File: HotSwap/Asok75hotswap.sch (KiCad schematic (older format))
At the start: 259 parts, among them J1 AVR-ISP-6, SW1 SW_Push, U1 ATmega32U4-MU, U2 PRTR5V0U2X, Y1 16MHz

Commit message: Removed extra symbols in schematic in hotswap variant
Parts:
- removed D12, D30, D52, D77: SOD-123, random-keyboard-parts:D_SOD-123-Pretty, symbol Device:D_Small
- removed MX_BCKSP2, MX_BCKSP3, MX_LSHIFT3, MX_LWIN2, MX_\2: MX-LED, MX_Only:MXOnly-1U-Hotswap, symbol MX_Alps_Hybrid:MX-LED
- removed MX_CAPS2, MX_LSHIFT2, MX_SPACE4: MX-LED, MX_Only:MXOnly-1.25U-Hotswap, symbol MX_Alps_Hybrid:MX-LED
- removed MX_ENTER2: MX-LED, MX_Only:MXOnly-ISO-ROTATED-ReversedStabilizers-NoLED, symbol MX_Alps_Hybrid:MX-LED
- removed MX_LALT2, MX_LALT3, MX_LCTRL2, MX_RALT2, MX_RCTRL2: MX-LED, MX_Only:MXOnly-1.5U-Hotswap, symbol MX_Alps_Hybrid:MX-LED
- removed MX_SPACE2, MX_SPACE3: MX-LED, MX_Only:MXOnly-7U-Hotswap-ReversedStabilizers, symbol MX_Alps_Hybrid:MX-LED
- removed MX_SPACE5: MX-LED, MX_Only:MXOnly-2.75U-Hotswap-ReversedStabilizers, symbol MX_Alps_Hybrid:MX-LED
- removed MX_SPACE6: MX-LED, MX_Only:MXOnly-2.25U-Hotswap-ReversedStabilizers, symbol MX_Alps_Hybrid:MX-LED
- C1: renamed from C21; footprint Capacitor_SMD:C_0805_2012Metric -> Capacitor_SMD:C_0603_1608Metric
- C10: renamed from C12; footprint Capacitor_SMD:C_0805_2012Metric -> Capacitor_SMD:C_0603_1608Metric
- C11: footprint Capacitor_SMD:C_0805_2012Metric -> Capacitor_SMD:C_0603_1608Metric
- C12: renamed from C10; footprint Capacitor_SMD:C_0805_2012Metric -> Capacitor_SMD:C_0603_1608Metric
- C13: renamed from C9; footprint Capacitor_SMD:C_0805_2012Metric -> Capacitor_SMD:C_0603_1608Metric
- C14: renamed from C8; footprint Capacitor_SMD:C_0805_2012Metric -> Capacitor_SMD:C_0603_1608Metric
- C15: renamed from C1; footprint Capacitor_SMD:C_0805_2012Metric -> Capacitor_SMD:C_0603_1608Metric
- C16: renamed from C2; footprint Capacitor_SMD:C_0805_2012Metric -> Capacitor_SMD:C_0603_1608Metric
- C17: renamed from C3; footprint Capacitor_SMD:C_0805_2012Metric -> Capacitor_SMD:C_0603_1608Metric
- C18: renamed from C4; footprint Capacitor_SMD:C_0805_2012Metric -> Capacitor_SMD:C_0603_1608Metric
- C19: renamed from C5; footprint Capacitor_SMD:C_0805_2012Metric -> Capacitor_SMD:C_0603_1608Metric
- C2: renamed from C20; footprint Capacitor_SMD:C_0805_2012Metric -> Capacitor_SMD:C_0603_1608Metric
- C20: renamed from C6; footprint Capacitor_SMD:C_0805_2012Metric -> Capacitor_SMD:C_0603_1608Metric
- C21: renamed from C7; footprint Capacitor_SMD:C_0805_2012Metric -> Capacitor_SMD:C_0603_1608Metric
- C3: renamed from C19; footprint Capacitor_SMD:C_0805_2012Metric -> Capacitor_SMD:C_0603_1608Metric
- C4: renamed from C18; footprint Capacitor_SMD:C_0805_2012Metric -> Capacitor_SMD:C_0603_1608Metric
- C5: renamed from C17; footprint Capacitor_SMD:C_0805_2012Metric -> Capacitor_SMD:C_0603_1608Metric
- C6: renamed from C16; footprint Capacitor_SMD:C_0805_2012Metric -> Capacitor_SMD:C_0603_1608Metric
- C7: renamed from C15; footprint Capacitor_SMD:C_0805_2012Metric -> Capacitor_SMD:C_0603_1608Metric
- C8: renamed from C14; footprint Capacitor_SMD:C_0805_2012Metric -> Capacitor_SMD:C_0603_1608Metric
- C9: renamed from C13; footprint Capacitor_SMD:C_0805_2012Metric -> Capacitor_SMD:C_0603_1608Metric
- R1, R2, R3: footprint Resistor_SMD:R_0805_2012Metric -> Resistor_SMD:R_0603_1608Metric
- R4: renamed from R7; footprint Resistor_SMD:R_0805_2012Metric -> Resistor_SMD:R_0603_1608Metric
- R5: renamed from R6; footprint Resistor_SMD:R_0805_2012Metric -> Resistor_SMD:R_0603_1608Metric
- R6: renamed from R5; footprint Resistor_SMD:R_0805_2012Metric -> Resistor_SMD:R_0603_1608Metric
- R7: renamed from R8; footprint Resistor_SMD:R_0805_2012Metric -> Resistor_SMD:R_0603_1608Metric
- R8: renamed from R9; footprint Resistor_SMD:R_0805_2012Metric -> Resistor_SMD:R_0603_1608Metric
- R9: renamed from R4; footprint Resistor_SMD:R_0805_2012Metric -> Resistor_SMD:R_0603_1608Metric
- renumbered D2 to D1, D11 to D10, D18 to D11, D13 to D12, D14 to D13, D15 to D14, D16 to D15, D17 to D16, D24 to D17, D19 to D18, D20 to D19, D3 to D2, D21 to D20, D22 to D21, D23 to D22, D29 to D23, D25 to D24, D26 to D25, D27 to D26, D28 to D27, D35 to D28, D31 to D29, D4 to D3, D32 to D30, D33 to D31, D34 to D32, D40 to D33, D36 to D34, D37 to D35, D38 to D36, D39 to D37, D46 to D38, D41 to D39, D5 to D4, D42 to D40, D43 to D41, D44 to D42, D45 to D43, D51 to D44, D47 to D45, D48 to D46, D49 to D47, D50 to D48, D57 to D49, D6 to D5, D53 to D50, D54 to D51, D55 to D52, D56 to D53, D63 to D54, D58 to D55, D59 to D56, D60 to D57, D61 to D58, D62 to D59, D7 to D6, D69 to D60, D64 to D61, D65 to D62, D66 to D63, D67 to D64, D68 to D65, D74 to D66, D70 to D67, D71 to D68, D72 to D69, D8 to D7, D73 to D70, D80 to D71, D81 to D72, D75 to D73, D76 to D74, D79 to D75, D78 to D76, D82 to D77, D83 to D78, D84 to D79, D9 to D8, D85 to D80, D89 to D81, D90 to D82, D91 to D83, D86 to D84, D87 to D85, D88 to D86, D1 to D87, D10 to D9, LED12 to LED10, LED6 to LED11, LED13 to LED12, LED7 to LED13, LED8 to LED2, LED2 to LED3, LED9 to LED4, LED3 to LED5, LED10 to LED6, LED4 to LED7, LED11 to LED8, LED5 to LED9, MX_#0 to MX_#10, U2 to U1, U1 to U2
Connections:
- net COL0: now also MX_Z1.1 (COL)
- net COL1: now also MX_C1.1 (COL); no longer MX_Z1.1 (COL)
- net COL2: now also MX_B1.1 (COL); no longer MX_C1.1 (COL)
- net COL3: now also MX_M1.1 (COL); no longer MX_B1.1 (COL)
- net COL4: now also MX_.1.1 (COL); no longer MX_M1.1 (COL)
- net COL5: now also MX_RSHIFT1.1 (COL); no longer MX_.1.1 (COL)
- net COL6: now also MX_BCKSP1.1 (COL), MX_DOWN1.1 (COL), MX_UP1.1 (COL); no longer MX_RSHIFT1.1 (COL)
- net COL7: no longer MX_BCKSP1.1 (COL), MX_DOWN1.1 (COL), MX_UP1.1 (COL)
- net ROW0: now also D78.1 (K)
- net ROW1: no longer D78.1 (K)
- net ROW10: now also D83.1 (K); no longer D77.1 (K)
- net ROW11: now also D77.1 (K); no longer D83.1 (K)
- net ROW2: now also D79.1 (K); no longer D75.1 (K)
- net ROW3: now also D75.1 (K); no longer D79.1 (K)
- net ROW4: now also D80.1 (K)
- net ROW5: no longer D80.1 (K)
- net ROW6: now also D81.1 (K)
- net ROW7: no longer D81.1 (K)
- net ROW8: now also D17.1 (K), D28.1 (K), D38.1 (K), D49.1 (K), D60.1 (K), D82.1 (K); no longer D11.1 (K), D23.1 (K), D33.1 (K), D44.1 (K), D54.1 (K), D66.1 (K)
- net ROW9: now also D11.1 (K), D23.1 (K), D33.1 (K), D44.1 (K), D54.1 (K), D66.1 (K); no longer D17.1 (K), D28.1 (K), D38.1 (K), D49.1 (K), D60.1 (K), D82.1 (K)
- net LEDMOS: now reaches U2.12 (PB7)
- net at MX_A1.3 (LED): now also MX_Z1.3 (LED)
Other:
- note added: "LED MOSFET\n"
- moved on the sheet: D11, D17, D23, D28, D33, D38, D44, D49, D54, D60, D66, D72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

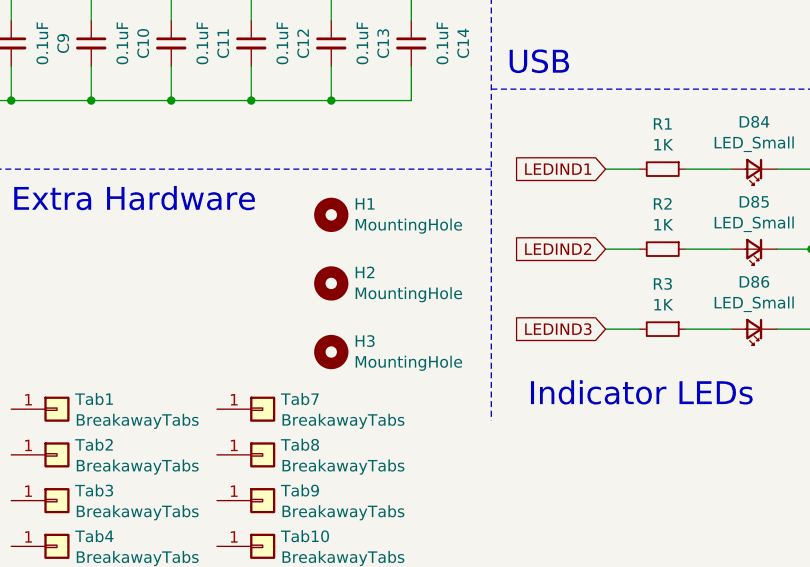
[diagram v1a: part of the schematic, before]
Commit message: Updated underglow LED footprint
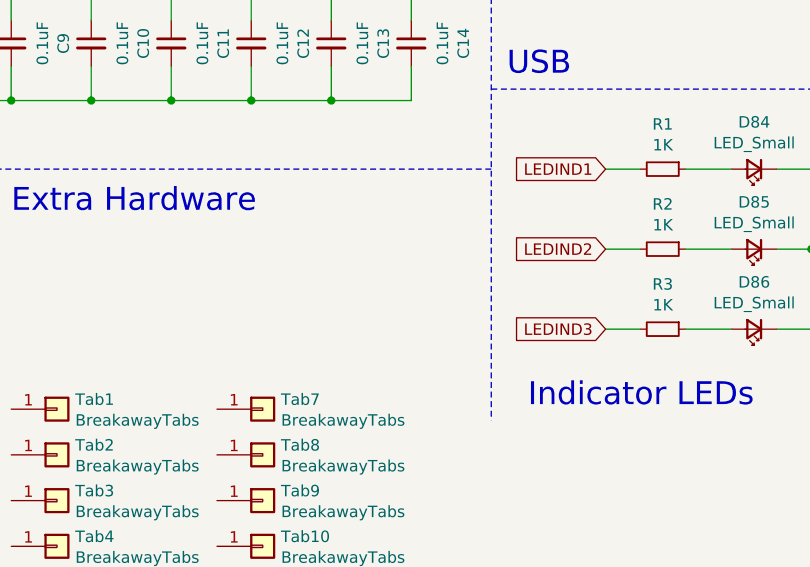
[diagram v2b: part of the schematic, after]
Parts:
- removed H1, H2, H3: MountingHole, mounting_hole:mounting, symbol Mechanical:MountingHole
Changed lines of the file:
@@
-	1    0    0    -1
-$EndComp
-$Comp
-L Mechanical:MountingHole H3
-U 1 1 5EBE734B
-P 11450 9650
-F 0 "H3" H 11550 9696 50  0000 L CNN
-F 1 "MountingHole" H 11550 9605 50  0000 L CNN
-F 2 "mounting_hole:mounting" H 11450 9650 50  0001 C CNN
-F 3 "~" H 11450 9650 50  0001 C CNN
-	1    11450 9650
-	1    0    0    -1
-$EndComp
-$Comp
-L Mechanical:MountingHole H2
-U 1 1 5EAF9D7C
-P 11450 9350
-F 0 "H2" H 11550 9396 50  0000 L CNN
-F 1 "MountingHole" H 11550 9305 50  0000 L CNN
-F 2 "mounting_hole:mounting" H 11450 9350 50  0001 C CNN
-F 3 "~" H 11450 9350 50  0001 C CNN
-	1    11450 9350
-	1    0    0    -1
-$EndComp
-$Comp
-L Mechanical:MountingHole H1
-U 1 1 5EAF6EE2
-P 11450 9050
-F 0 "H1" H 11550 9096 50  0000 L CNN
-F 1 "MountingHole" H 11550 9005 50  0000 L CNN
-F 2 "mounting_hole:mounting" H 11450 9050 50  0001 C CNN
-F 3 "~" H 11450 9050 50  0001 C CNN
-	1    11450 9050
 	1    0    0    -1
 $EndComp

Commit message: Routed USB and MCU area for hotswap version
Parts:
- removed D87: Schottky, random-keyboard-parts:D_SOD-123-Pretty, symbol Device:D_Schottky_Small
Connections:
- net +5V: now also F1.1
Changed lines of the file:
@@
 	1    0    0    -1
 $EndComp
-$Comp
-L Device:D_Schottky_Small D87
-U 1 1 617B5949
-P 14050 5800
-F 0 "D87" H 14050 5595 50  0000 C CNN
-F 1 "Schottky" H 14050 5686 50  0000 C CNN
-F 2 "random-keyboard-parts:D_SOD-123-Pretty" V 14050 5800 50  0001 C CNN
-F 3 "~" V 14050 5800 50  0001 C CNN
-	1    14050 5800
-	-1   0    0    1
-$EndComp
-Wire Wire Line
-	13800 5800 13950 5800
-Wire Wire Line
-	14150 5800 14250 5800
 Wire Wire Line
 	14250 5800 14250 5700
@@
 Wire Wire Line
 	8900 2700 10200 2700
+Wire Wire Line
+	13800 5800 14250 5800
 $EndSCHEMATC

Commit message: Routed underglow LEDs
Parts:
- renumbered LED6 to LED10, LED8 to LED11, LED10 to LED12, LED12 to LED13, LED3 to LED2, LED5 to LED3, LED7 to LED4, LED9 to LED5, LED11 to LED6, LED13 to LED7, LED2 to LED8, LED4 to LED9
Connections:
- net COL0: no longer U2.32 (PC7)
- net COL1: no longer U2.31 (PC6)
- net COL2: no longer U2.30 (PB6)
- net COL3: no longer U2.29 (PB5)
- net COL4: no longer U2.28 (PB4)
- net COL5: no longer U2.27 (PD7)
- net COL6: no longer U2.26 (PD6)
- net COL7: no longer U2.25 (PD4)
- net LEDIND1: no longer U2.10 (PB2)
- net LEDIND2: no longer U2.9 (PB1)
- net LEDIND3: no longer U2.8 (PB0)
- net RGBLED: no longer U2.18 (PD0)
- net ROW0: no longer U2.1 (PE6)
- net ROW1: no longer U2.11 (PB3)
- net ROW10: no longer U2.20 (PD2)
- net ROW11: no longer U2.19 (PD1)
- net ROW2: no longer U2.41 (PF0)
- net ROW3: no longer U2.40 (PF1)
- net ROW4: no longer U2.39 (PF4)
- net ROW5: no longer U2.38 (PF5)
- net ROW6: no longer U2.37 (PF6)
- net ROW7: no longer U2.36 (PF7)
- net ROW8: no longer U2.21 (PD3)
- net ROW9: no longer U2.22 (PD5)
- net LEDMOS: no longer names the net of U2.12 (PB7)
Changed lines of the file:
@@
 Text Notes 8050 7700 0    100  ~ 0
 Underglow LEDs
-Text GLabel 15450 1900 2    50   Input ~ 0
-LEDMOS
 $Comp
 L power:GND #PWR017
@@
 Connection ~ 8650 8550
 Connection ~ 9000 8050
-Text GLabel 15450 2200 2    50   Input ~ 0
-COL0
-Text GLabel 15450 2100 2    50   Input ~ 0
-COL1
-Text GLabel 15450 1800 2    50   Input ~ 0
-COL2
-Text GLabel 15450 1700 2    50   Input ~ 0
-COL3
-Text GLabel 15450 1600 2    50   Input ~ 0
-COL4
-Text GLabel 15450 3100 2    50   Input ~ 0
-COL5
-Text GLabel 15450 3000 2    50   Input ~ 0
-COL6
-Text GLabel 15450 2800 2    50   Input ~ 0
-COL7
-Text GLabel 15450 2400 2    50   Input ~ 0
-RGBLED
-Text GLabel 15450 2600 2    50   Input ~ 0
-ROW10
-Text GLabel 15450 2500 2    50   Input ~ 0
-ROW11
-Text GLabel 15450 2900 2    50   Input ~ 0
-ROW9
-Text GLabel 15450 2700 2    50   Input ~ 0
-ROW8
-Text GLabel 15450 4100 2    50   Input ~ 0
-ROW7
-Text GLabel 15450 4000 2    50   Input ~ 0
-ROW6
-Text GLabel 15450 3900 2    50   Input ~ 0
-ROW5
-Text GLabel 15450 3800 2    50   Input ~ 0
-ROW4
-Text GLabel 15450 3600 2    50   Input ~ 0
-ROW2
-Text GLabel 15450 3700 2    50   Input ~ 0
-ROW3
-Text GLabel 15450 1500 2    50   Input ~ 0
-ROW1
-Text GLabel 15450 3400 2    50   Input ~ 0
-ROW0
-Text GLabel 15450 1400 2    50   Input ~ 0
-LEDIND1
-Text GLabel 15450 1300 2    50   Input ~ 0
-LEDIND2
-Text GLabel 15450 1200 2    50   Input ~ 0
-LEDIND3
 Text Notes 15850 1350 0    50   ~ 0
 SCK\n
@@
 $EndComp
 $Comp
-L asok75:SK6812-SIDEA-4020 LED3
+L asok75:SK6812-SIDEA-4020 LED2
 U 1 1 5F5065E5
 P 2650 9450
-F 0 "LED3" H 2650 9937 60  0000 C CNN
+F 0 "LED2" H 2650 9937 60  0000 C CNN
 F 1 "SK6812-SIDEA-4020" H 2650 9831 60  0000 C CNN
 F 2 "asok75:SK6812-SIDEA-4020" V 2600 9450 60  0001 C CNN
@@
 $EndComp
 $Comp
-L asok75:SK6812-SIDEA-4020 LED5
+L asok75:SK6812-SIDEA-4020 LED3
 U 1 1 5F50BC5A
 P 3950 9450
-F 0 "LED5" H 3950 9937 60  0000 C CNN
+F 0 "LED3" H 3950 9937 60  0000 C CNN
 F 1 "SK6812-SIDEA-4020" H 3950 9831 60  0000 C CNN
 F 2 "asok75:SK6812-SIDEA-4020" V 3900 9450 60  0001 C CNN
@@
 $EndComp
 $Comp
-L asok75:SK6812-SIDEA-4020 LED7
+L asok75:SK6812-SIDEA-4020 LED4
 U 1 1 5F5CE02B
 P 5250 9450
-F 0 "LED7" H 5250 9937 60  0000 C CNN
+F 0 "LED4" H 5250 9937 60  0000 C CNN
 F 1 "SK6812-SIDEA-4020" H 5250 9831 60  0000 C CNN
 F 2 "asok75:SK6812-SIDEA-4020" V 5200 9450 60  0001 C CNN
@@
 $EndComp
 $Comp
-L asok75:SK6812-SIDEA-4020 LED9
+L asok75:SK6812-SIDEA-4020 LED5
 U 1 1 5F68F568
 P 6550 9450
-F 0 "LED9" H 6550 9937 60  0000 C CNN
+F 0 "LED5" H 6550 9937 60  0000 C CNN
 F 1 "SK6812-SIDEA-4020" H 6550 9831 60  0000 C CNN
 F 2 "asok75:SK6812-SIDEA-4020" V 6500 9450 60  0001 C CNN
@@
 $EndComp
 $Comp
-L asok75:SK6812-SIDEA-4020 LED11
+L asok75:SK6812-SIDEA-4020 LED6
 U 1 1 5F750D68
 P 7850 9450
-F 0 "LED11" H 7850 9937 60  0000 C CNN
+F 0 "LED6" H 7850 9937 60  0000 C CNN
 F 1 "SK6812-SIDEA-4020" H 7850 9831 60  0000 C CNN
 F 2 "asok75:SK6812-SIDEA-4020" V 7800 9450 60  0001 C CNN
@@
 $EndComp
 $Comp
-L asok75:SK6812-SIDEA-4020 LED13
+L asok75:SK6812-SIDEA-4020 LED7
 U 1 1 5F811FD6
 P 9150 9450
-F 0 "LED13" H 9150 9937 60  0000 C CNN
+F 0 "LED7" H 9150 9937 60  0000 C CNN
 F 1 "SK6812-SIDEA-4020" H 9150 9831 60  0000 C CNN
 F 2 "asok75:SK6812-SIDEA-4020" V 9100 9450 60  0001 C CNN
@@
 $EndComp
 $Comp
-L asok75:SK6812-SIDEA-4020 LED4
+L asok75:SK6812-SIDEA-4020 LED9
 U 1 1 5FA6047D
 P 2650 10450
-F 0 "LED4" H 2650 10937 60  0000 C CNN
+F 0 "LED9" H 2650 10937 60  0000 C CNN
 F 1 "SK6812-SIDEA-4020" H 2650 10831 60  0000 C CNN
 F 2 "asok75:SK6812-SIDEA-4020" V 2600 10450 60  0001 C CNN
@@
 $EndComp
 $Comp
-L asok75:SK6812-SIDEA-4020 LED6
+L asok75:SK6812-SIDEA-4020 LED10
 U 1 1 5FA60483
 P 3950 10450
-F 0 "LED6" H 3950 10937 60  0000 C CNN
+F 0 "LED10" H 3950 10937 60  0000 C CNN
 F 1 "SK6812-SIDEA-4020" H 3950 10831 60  0000 C CNN
 F 2 "asok75:SK6812-SIDEA-4020" V 3900 10450 60  0001 C CNN
@@
 $EndComp
 $Comp
-L asok75:SK6812-SIDEA-4020 LED8
+L asok75:SK6812-SIDEA-4020 LED11
 U 1 1 5FA60489
 P 5250 10450
-F 0 "LED8" H 5250 10937 60  0000 C CNN
+F 0 "LED11" H 5250 10937 60  0000 C CNN
 F 1 "SK6812-SIDEA-4020" H 5250 10831 60  0000 C CNN
 F 2 "asok75:SK6812-SIDEA-4020" V 5200 10450 60  0001 C CNN
@@
 $EndComp
 $Comp
-L asok75:SK6812-SIDEA-4020 LED10
+L asok75:SK6812-SIDEA-4020 LED12
 U 1 1 5FA6048F
 P 6550 10450
-F 0 "LED10" H 6550 10937 60  0000 C CNN
+F 0 "LED12" H 6550 10937 60  0000 C CNN
 F 1 "SK6812-SIDEA-4020" H 6550 10831 60  0000 C CNN
 F 2 "asok75:SK6812-SIDEA-4020" V 6500 10450 60  0001 C CNN
@@
 $EndComp
 $Comp
-L asok75:SK6812-SIDEA-4020 LED12
+L asok75:SK6812-SIDEA-4020 LED13
 U 1 1 5FA60495
 P 7850 10450
-F 0 "LED12" H 7850 10937 60  0000 C CNN
+F 0 "LED13" H 7850 10937 60  0000 C CNN
 F 1 "SK6812-SIDEA-4020" H 7850 10831 60  0000 C CNN
 F 2 "asok75:SK6812-SIDEA-4020" V 7800 10450 60  0001 C CNN
@@
 $EndComp
 $Comp
-L asok75:SK6812-SIDEA-4020 LED2
+L asok75:SK6812-SIDEA-4020 LED8
 U 1 1 5FA604A1
 P 1350 10450
-F 0 "LED2" H 1350 10937 60  0000 C CNN
+F 0 "LED8" H 1350 10937 60  0000 C CNN
 F 1 "SK6812-SIDEA-4020" H 1350 10831 60  0000 C CNN
 F 2 "asok75:SK6812-SIDEA-4020" V 1300 10450 60  0001 C CNN

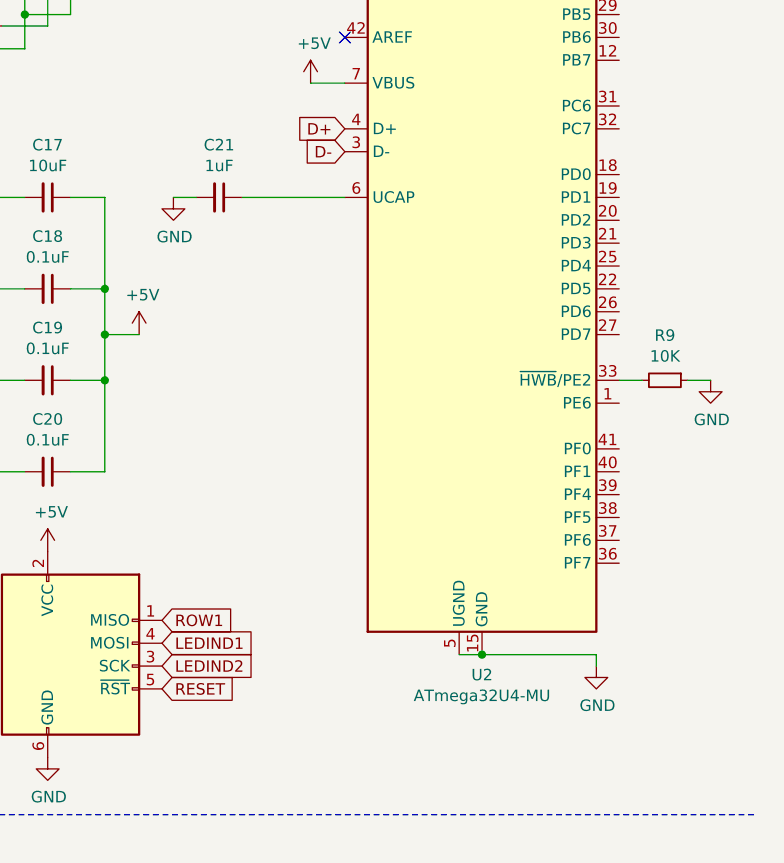
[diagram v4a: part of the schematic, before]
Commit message: Finished routing underglow LED power traces
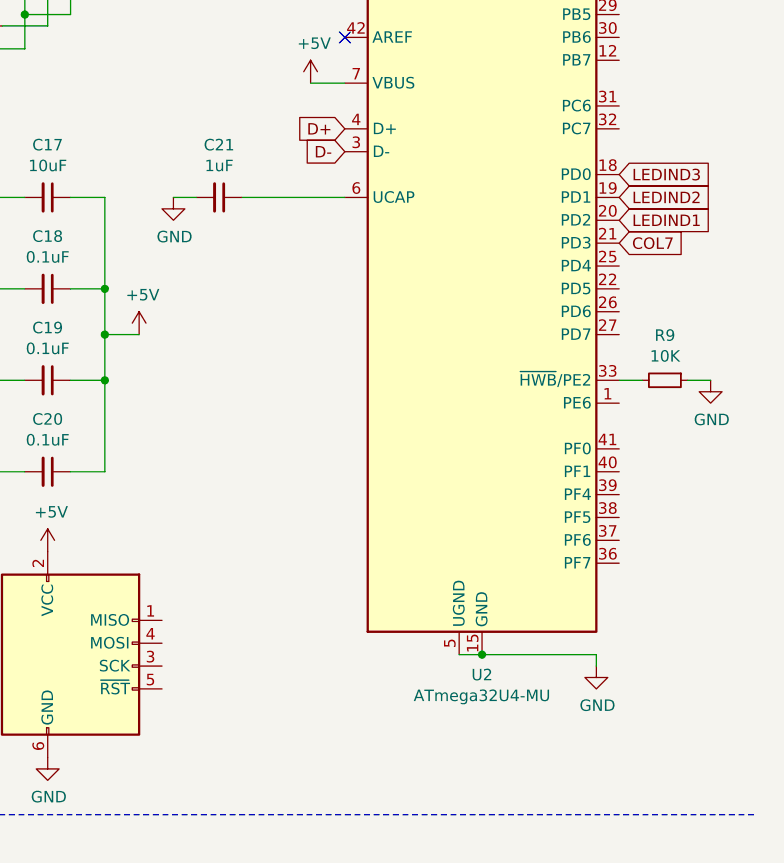
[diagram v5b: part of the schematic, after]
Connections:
- net COL7: now also U2.21 (PD3)
- net LEDIND1: now also U2.20 (PD2); no longer J1.4 (MOSI)
- net LEDIND2: now also U2.19 (PD1); no longer J1.3 (SCK)
- net LEDIND3: now also U2.18 (PD0)
- net RESET: no longer J1.5 (~RST)
- net ROW1: no longer J1.1 (MISO)
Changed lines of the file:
@@
 	1    0    0    -1
 $EndComp
-Text GLabel 13450 4650 2    50   Input ~ 0
-RESET
-Text GLabel 13450 4550 2    50   Input ~ 0
-LEDIND2
-Text GLabel 13450 4450 2    50   Input ~ 0
-LEDIND1
-Text GLabel 13450 4350 2    50   Input ~ 0
-ROW1
 $Comp
 L power:GND #PWR08
@@
 Wire Wire Line
 	13800 5800 14250 5800
+Text GLabel 15450 2600 2    50   Input ~ 0
+LEDIND1
+Text GLabel 15450 2700 2    50   Input ~ 0
+COL7
+Text GLabel 15450 2500 2    50   Input ~ 0
+LEDIND2
+Text GLabel 15450 2400 2    50   Input ~ 0
+LEDIND3
 $EndSCHEMATC

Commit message: Finished routing hotswap version
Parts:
- removed Tab10, Tab11, Tab12, Tab13, Tab5, Tab6, Tab7, Tab8, Tab9: BreakawayTabs, random-keyboard-parts:breakaway-mousebites, symbol Connector_Generic:Conn_01x01
- renumbered C17 to C1, C12 to C10, C10 to C12, C9 to C13, C8 to C14, C7 to C15, C6 to C16, C5 to C17, C4 to C18, C3 to C19, C18 to C2, C2 to C20, C1 to C21, C19 to C3, C20 to C4, C21 to C5, C15 to C6, C16 to C7, C14 to C8, C13 to C9, D84 to LED1, D85 to LED2, D86 to LED3, MX_BCKSP1 to MX_BACK1, R9 to R1, R6 to R2, R8 to R3, R7 to R4, R4 to R6, R1 to R7, R2 to R8, R3 to R9, LED1 to RGB1, LED10 to RGB10, LED11 to RGB11, LED12 to RGB12, LED13 to RGB13, LED14 to RGB14, LED2 to RGB2, LED3 to RGB3, LED4 to RGB4, LED5 to RGB5, LED6 to RGB6, LED7 to RGB7, LED8 to RGB8, LED9 to RGB9, U2 to U1, U1 to U2
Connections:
- net COL0: now also J1.4 (MOSI), U1.10 (PB2)
- net COL1: now also J1.3 (SCK), U1.9 (PB1)
- net COL2: now also U1.8 (PB0)
- net COL3: now also U1.40 (PF1)
- net COL4: now also U1.39 (PF4)
- net COL5: now also U1.38 (PF5)
- net COL6: now also U1.37 (PF6)
- net RESET: now also J1.5 (~RST)
- net RGBLED: now also U1.27 (PD7)
- net ROW0: now also U1.12 (PB7)
- net ROW1: now also J1.1 (MISO), U1.11 (PB3)
- net ROW10: now also U1.29 (PB5)
- net ROW11: now also U1.28 (PB4)
- net ROW2: now also U1.25 (PD4)
- net ROW3: now also U1.26 (PD6)
- net ROW4: now also U1.1 (PE6)
- net ROW5: now also U1.41 (PF0)
- net ROW6: now also U1.31 (PC6)
- net ROW7: now also U1.30 (PB6)
- net ROW8: now also U1.36 (PF7)
- net ROW9: now also U1.32 (PC7)
